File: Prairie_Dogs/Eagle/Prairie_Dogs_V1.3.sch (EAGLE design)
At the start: 19 parts, among them Q1 MOSFET-NCH, U1 ITSYBITSY_5V, X1 PHOENIX_508_3PIN

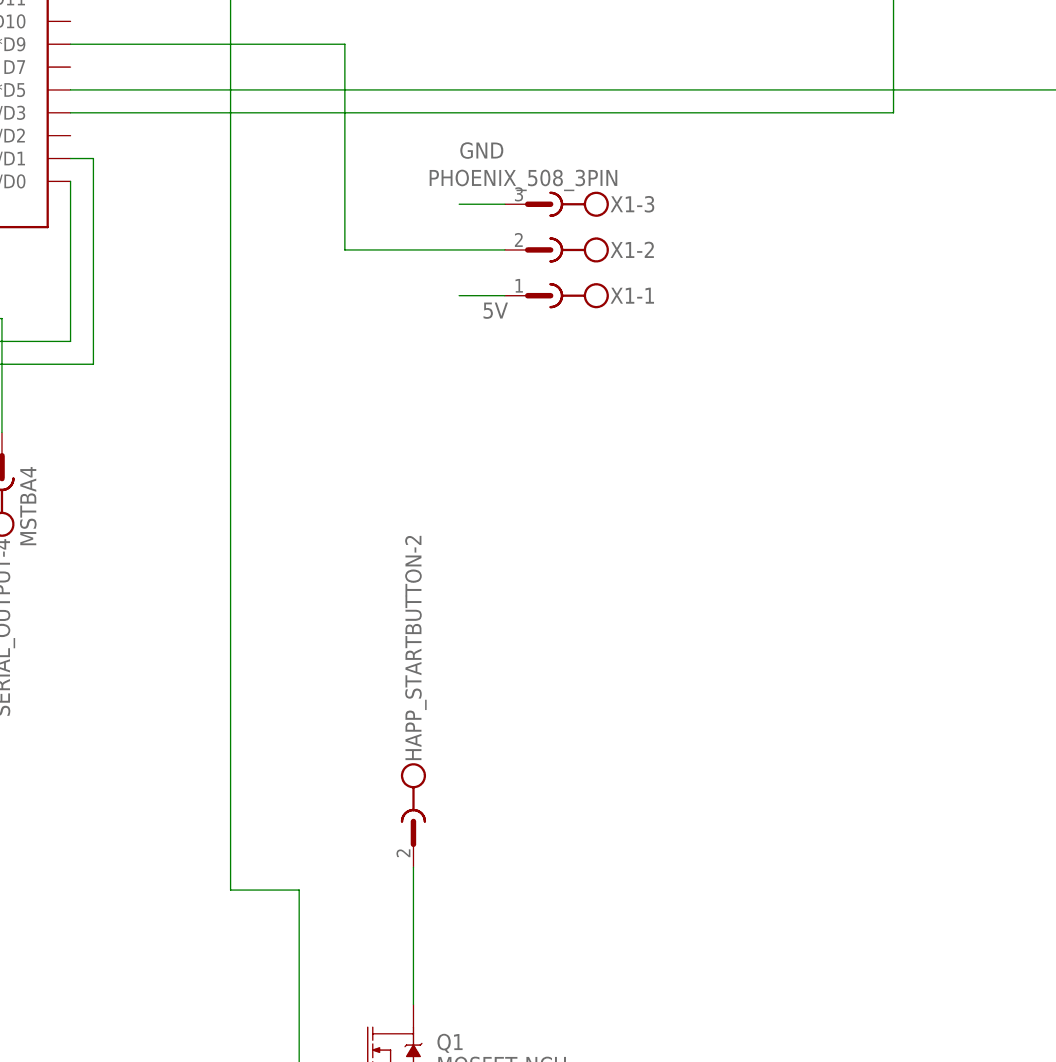
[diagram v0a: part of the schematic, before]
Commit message: changed the direction of lights and logic
instead of having one array that is broken up into pointers and then manually changed we break up the large array into smaller ones and then address each one seperately
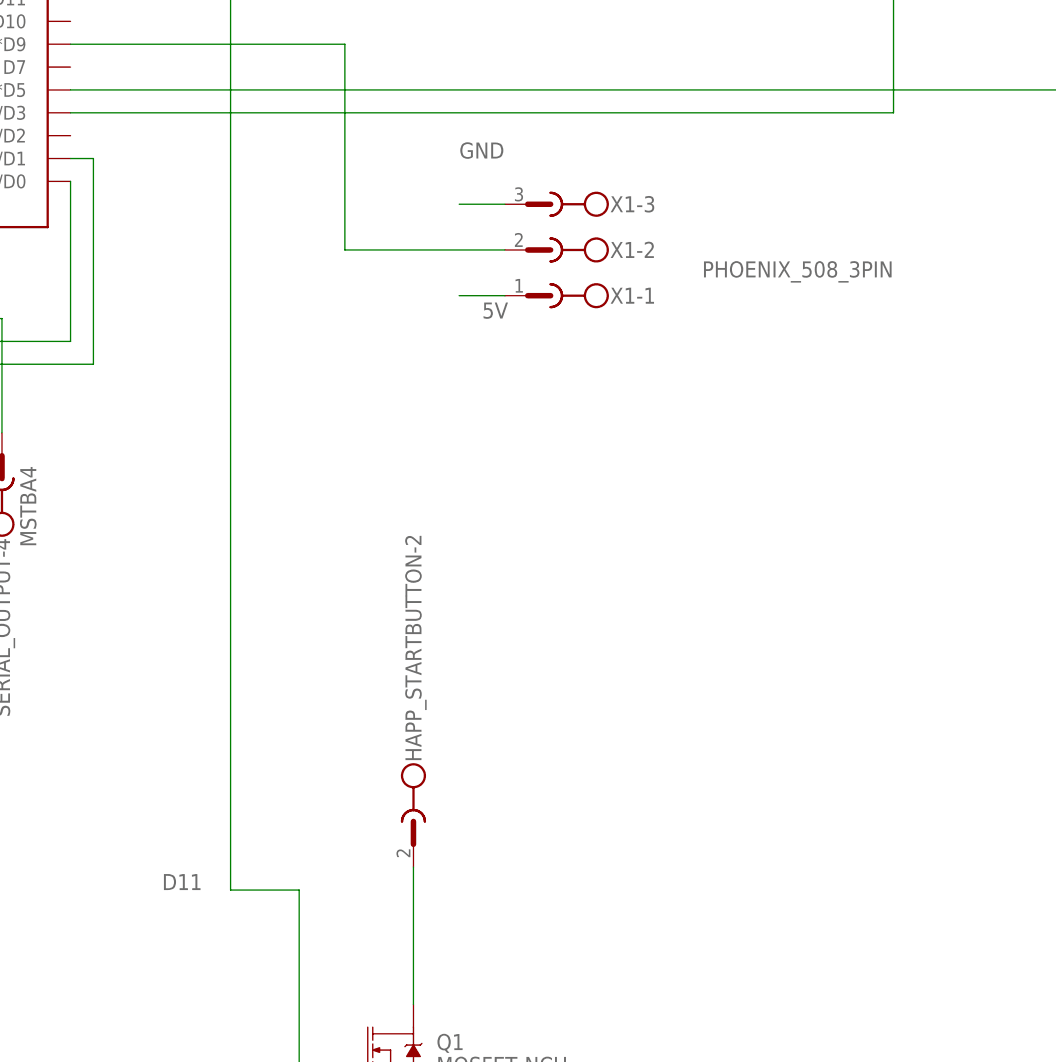
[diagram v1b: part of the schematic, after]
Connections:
- net N$9 renamed D11
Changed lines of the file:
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@@
 </instance>
 <instance part="X1" gate="-3" x="167.64" y="127" smashed="yes" rot="R180">
-<attribute name="VALUE" x="175.26" y="130.81" size="1.778" layer="96" rot="R180"/>
+<attribute name="VALUE" x="205.74" y="120.65" size="1.778" layer="96" rot="R180"/>
 <attribute name="NAME" x="174.244" y="126.111" size="1.778" layer="95"/>
 </instance>
@@
 </segment>
 </net>
-<net name="N$9" class="0">
+<net name="D11" class="0">
 <segment>
 <wire x1="132.08" y1="50.8" x2="139.7" y2="50.8" width="0.1524" layer="91"/>
@@
 <pinref part="10K" gate="G$1" pin="2"/>
 <wire x1="139.7" y1="25.4" x2="139.7" y2="50.8" width="0.1524" layer="91"/>
+<label x="124.46" y="50.8" size="1.778" layer="95"/>
 </segment>
 </net>
